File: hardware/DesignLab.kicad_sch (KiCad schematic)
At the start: 77 parts, among them J1 Micro_SD_Card_Det, J2 Conn_01x04_Female, J3 Conn_01x05, J5 Conn_01x05, P1 USB_C_Plug_USB2.0, Q1 DMG3415U-7, SW1 SW_DPDT_x2, SW11 SW_DPDT_x2, SW12 RESET, SW13 ON, SW14 VOL, SW15 BOOT, SW3 REC, U1 SPH0641LM4H, U10 MCP4018-xxxxLT, U2 RP2040, U3 QRE1113, U4 QRE1113, U5 QRE1113, U6 W25Q80DVSSIG, U7 PAM8302AASCR, U8 AP2112K-3.3, U9 QRE1113, Y1 12Mhz

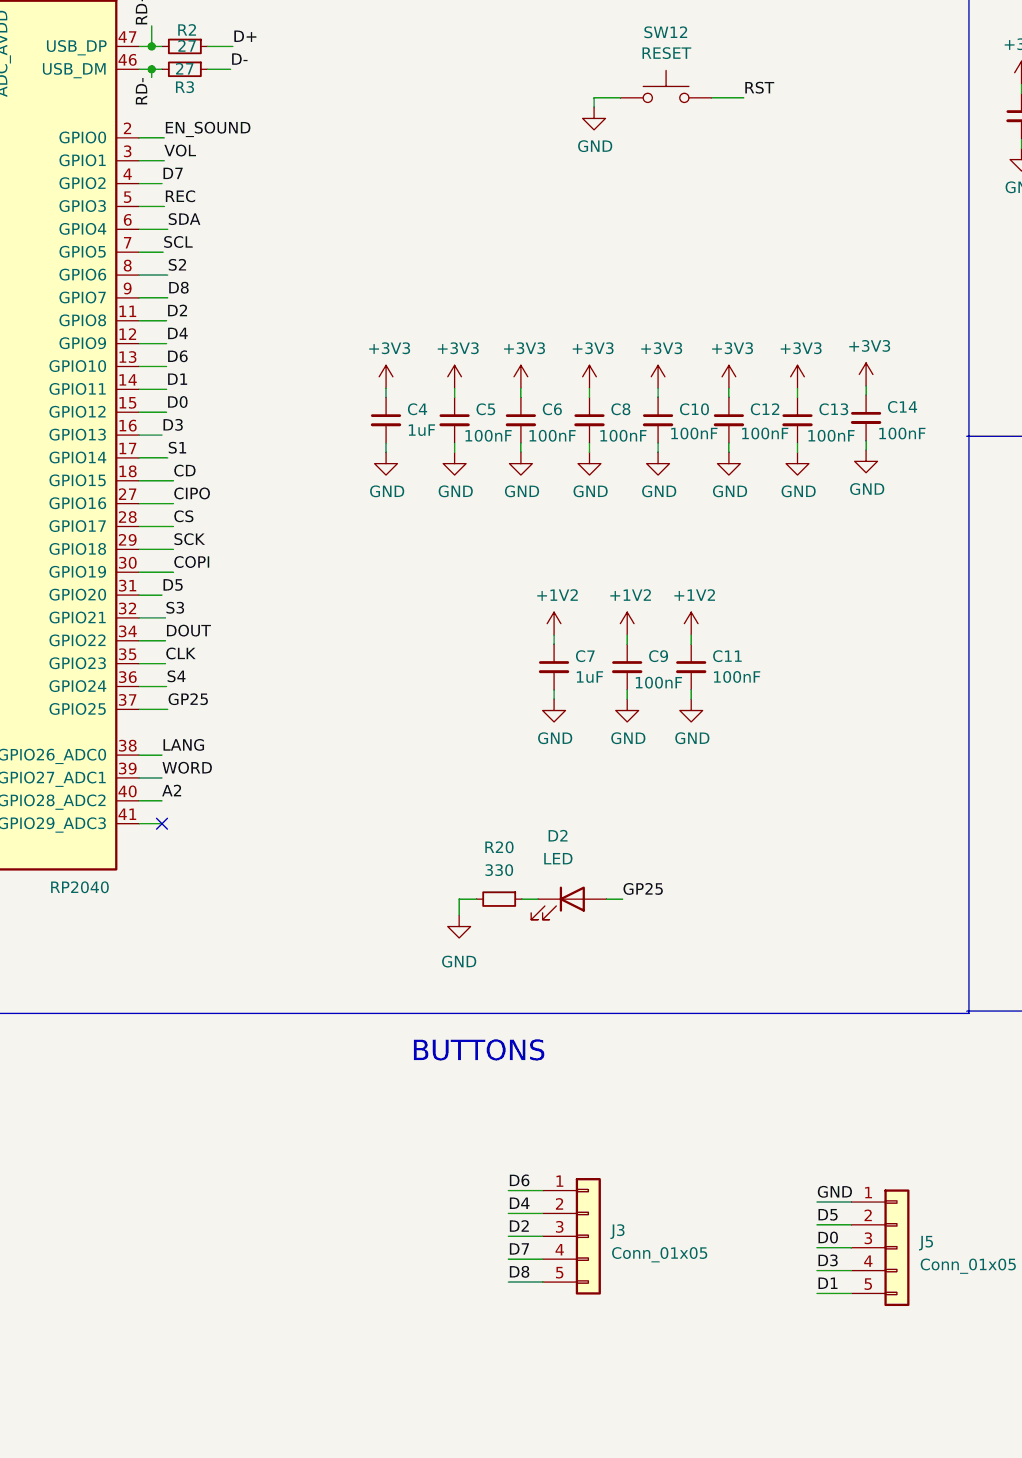
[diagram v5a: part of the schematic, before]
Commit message: PCB routing finished
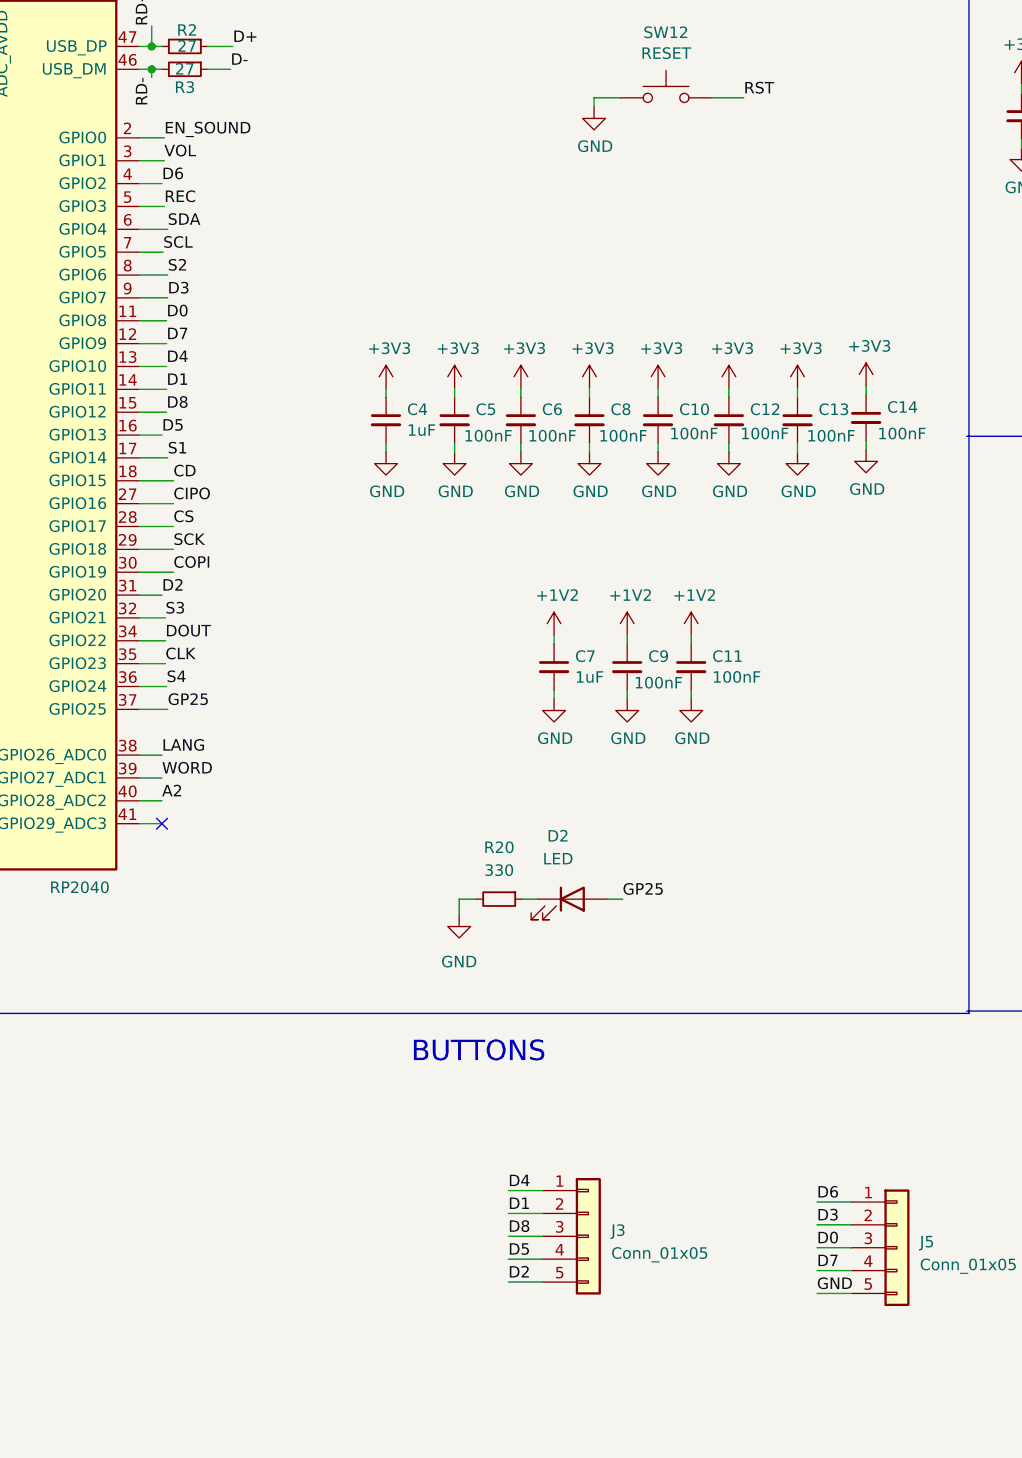
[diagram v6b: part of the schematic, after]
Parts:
- J3, J5: footprint (none) -> Connector_PinHeader_2.54mm:PinHeader_1x05_P2.54mm_Vertical
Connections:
- net D0: now also U2.11 (GPIO8); no longer U2.15 (GPIO12)
- net D1: now also J3.2 (Pin_2); no longer J5.5 (Pin_5)
- net D2: now also J3.5 (Pin_5), U2.31 (GPIO20); no longer J3.3 (Pin_3), U2.11 (GPIO8)
- net D3: now also J5.2 (Pin_2), U2.9 (GPIO7); no longer J5.4 (Pin_4), U2.16 (GPIO13)
- net D4: now also J3.1 (Pin_1), U2.13 (GPIO10); no longer J3.2 (Pin_2), U2.12 (GPIO9)
- net D5: now also J3.4 (Pin_4), U2.16 (GPIO13); no longer J5.2 (Pin_2), U2.31 (GPIO20)
- net D6: now also J5.1 (Pin_1), U2.4 (GPIO2); no longer J3.1 (Pin_1), U2.13 (GPIO10)
- net D7: now also J5.4 (Pin_4), U2.12 (GPIO9); no longer J3.4 (Pin_4), U2.4 (GPIO2)
- net D8: now also J3.3 (Pin_3), U2.15 (GPIO12); no longer J3.5 (Pin_5), U2.9 (GPIO7)
- net GND: now also J5.5 (Pin_5); no longer J5.1 (Pin_1)
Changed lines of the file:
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@@
     (effects (font (size 1.27 1.27)) (justify left bottom))
   )
-  (label "D0" (at 114.427 78.613 0) (fields_autoplaced)
+  (label "D8" (at 114.427 78.613 0) (fields_autoplaced)
     (effects (font (size 1.27 1.27)) (justify left bottom))
   )
@@
     (effects (font (size 1.27 1.27)) (justify left bottom))
   )
-  (label "D2" (at 114.427 68.453 0) (fields_autoplaced)
+  (label "D0" (at 114.427 68.453 0) (fields_autoplaced)
     (effects (font (size 1.27 1.27)) (justify left bottom))
   )
-  (label "D8" (at 152.4 175.26 0) (fields_autoplaced)
+  (label "D2" (at 152.4 175.26 0) (fields_autoplaced)
     (effects (font (size 1.27 1.27)) (justify left bottom))
   )
-  (label "D2" (at 152.4 170.18 0) (fields_autoplaced)
+  (label "D8" (at 152.4 170.18 0) (fields_autoplaced)
     (effects (font (size 1.27 1.27)) (justify left bottom))
   )
-  (label "D7" (at 152.4 172.72 0) (fields_autoplaced)
+  (label "D5" (at 152.4 172.72 0) (fields_autoplaced)
     (effects (font (size 1.27 1.27)) (justify left bottom))
   )
@@
     (effects (font (size 1.27 1.27)) (justify left bottom))
   )
-  (label "D3" (at 186.69 173.99 0) (fields_autoplaced)
+  (label "D7" (at 186.69 173.99 0) (fields_autoplaced)
     (effects (font (size 1.27 1.27)) (justify left bottom))
   )
@@
     (effects (font (size 1.27 1.27)) (justify left bottom))
   )
-  (label "D6" (at 152.4 165.1 0) (fields_autoplaced)
+  (label "D4" (at 152.4 165.1 0) (fields_autoplaced)
     (effects (font (size 1.27 1.27)) (justify left bottom))
   )
@@
     (effects (font (size 1.27 1.27)) (justify right bottom))
   )
-  (label "GND" (at 186.69 166.37 0) (fields_autoplaced)
+  (label "D6" (at 186.69 166.37 0) (fields_autoplaced)
     (effects (font (size 1.27 1.27)) (justify left bottom))
   )
@@
     (effects (font (size 1.27 1.27)) (justify left bottom))
   )
-  (label "D5" (at 186.69 168.91 0) (fields_autoplaced)
+  (label "D3" (at 186.69 168.91 0) (fields_autoplaced)
     (effects (font (size 1.27 1.27)) (justify left bottom))
   )
@@
     (effects (font (size 1.27 1.27)) (justify right bottom))
   )
-  (label "D7" (at 113.919 53.213 0) (fields_autoplaced)
+  (label "D6" (at 113.919 53.213 0) (fields_autoplaced)
     (effects (font (size 1.27 1.27)) (justify left bottom))
   )
-  (label "D4" (at 152.4 167.64 0) (fields_autoplaced)
+  (label "D1" (at 152.4 167.64 0) (fields_autoplaced)
     (effects (font (size 1.27 1.27)) (justify left bottom))
   )
@@
     (effects (font (size 1.27 1.27)) (justify left bottom))
   )
-  (label "D1" (at 186.69 176.53 0) (fields_autoplaced)
+  (label "GND" (at 186.69 176.53 0) (fields_autoplaced)
     (effects (font (size 1.27 1.27)) (justify left bottom))
   )
@@
     (effects (font (size 1.27 1.27)) (justify left bottom))
   )
-  (label "D4" (at 114.427 70.993 0) (fields_autoplaced)
+  (label "D7" (at 114.427 70.993 0) (fields_autoplaced)
     (effects (font (size 1.27 1.27)) (justify left bottom))
   )
@@
     (effects (font (size 1.27 1.27)) (justify left bottom))
   )
-  (label "D8" (at 114.554 65.913 0) (fields_autoplaced)
+  (label "D3" (at 114.554 65.913 0) (fields_autoplaced)
     (effects (font (size 1.27 1.27)) (justify left bottom))
   )
@@
     (effects (font (size 1.27 1.27)) (justify left bottom))
   )
-  (label "D5" (at 113.919 98.933 0) (fields_autoplaced)
+  (label "D2" (at 113.919 98.933 0) (fields_autoplaced)
     (effects (font (size 1.27 1.27)) (justify left bottom))
   )
@@
     (effects (font (size 1.27 1.27)) (justify left bottom))
   )
-  (label "D3" (at 113.919 81.153 0) (fields_autoplaced)
+  (label "D5" (at 113.919 81.153 0) (fields_autoplaced)
     (effects (font (size 1.27 1.27)) (justify left bottom))
   )
@@
     (effects (font (size 1.27 1.27)) (justify left bottom))
   )
-  (label "D6" (at 114.427 73.533 0) (fields_autoplaced)
+  (label "D4" (at 114.427 73.533 0) (fields_autoplaced)
     (effects (font (size 1.27 1.27)) (justify left bottom))
   )
@@
       (effects (font (size 1.27 1.27)) (justify left))
     )
-    (property "Footprint" "" (at 161.29 170.18 0)
+    (property "Footprint" "Connector_PinHeader_2.54mm:PinHeader_1x05_P2.54mm_Vertical" (at 161.29 170.18 0)
       (effects (font (size 1.27 1.27)) hide)
     )
@@
       (effects (font (size 1.27 1.27)) (justify left))
     )
-    (property "Footprint" "" (at 195.58 171.45 0)
+    (property "Footprint" "Connector_PinHeader_2.54mm:PinHeader_1x05_P2.54mm_Vertical" (at 195.58 171.45 0)
       (effects (font (size 1.27 1.27)) hide)
     )

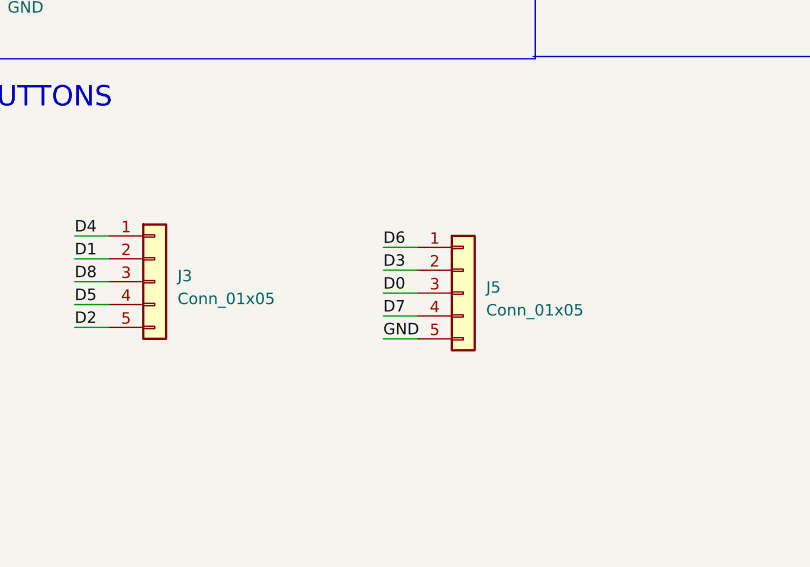
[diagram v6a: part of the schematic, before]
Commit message: Finished button PCBs
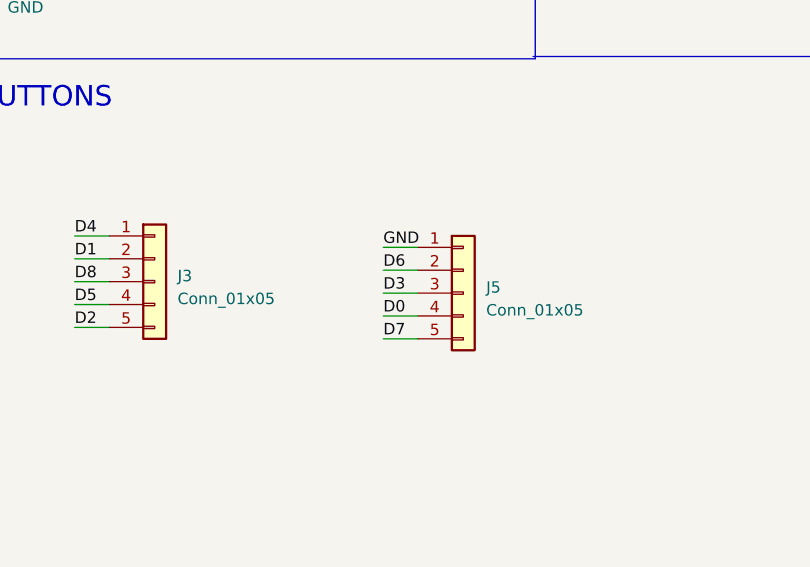
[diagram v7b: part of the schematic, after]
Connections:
- net D0: now also J5.4 (Pin_4); no longer J5.3 (Pin_3)
- net D3: now also J5.3 (Pin_3); no longer J5.2 (Pin_2)
- net D6: now also J5.2 (Pin_2); no longer J5.1 (Pin_1)
- net D7: now also J5.5 (Pin_5); no longer J5.4 (Pin_4)
- net GND: now also J5.1 (Pin_1); no longer J5.5 (Pin_5)
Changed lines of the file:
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@@
     (effects (font (size 1.27 1.27)) (justify left bottom))
   )
-  (label "D7" (at 186.69 173.99 0) (fields_autoplaced)
+  (label "D0" (at 186.69 173.99 0) (fields_autoplaced)
     (effects (font (size 1.27 1.27)) (justify left bottom))
   )
@@
     (effects (font (size 1.27 1.27)) (justify right bottom))
   )
-  (label "D6" (at 186.69 166.37 0) (fields_autoplaced)
+  (label "GND" (at 186.69 166.37 0) (fields_autoplaced)
     (effects (font (size 1.27 1.27)) (justify left bottom))
   )
@@
     (effects (font (size 1.27 1.27)) (justify left bottom))
   )
-  (label "D3" (at 186.69 168.91 0) (fields_autoplaced)
+  (label "D6" (at 186.69 168.91 0) (fields_autoplaced)
     (effects (font (size 1.27 1.27)) (justify left bottom))
   )
@@
     (effects (font (size 1.27 1.27)) (justify left bottom))
   )
-  (label "GND" (at 186.69 176.53 0) (fields_autoplaced)
+  (label "D7" (at 186.69 176.53 0) (fields_autoplaced)
     (effects (font (size 1.27 1.27)) (justify left bottom))
   )
@@
     (effects (font (size 1.27 1.27)) (justify left bottom))
   )
-  (label "D0" (at 186.69 171.45 0) (fields_autoplaced)
+  (label "D3" (at 186.69 171.45 0) (fields_autoplaced)
     (effects (font (size 1.27 1.27)) (justify left bottom))
   )

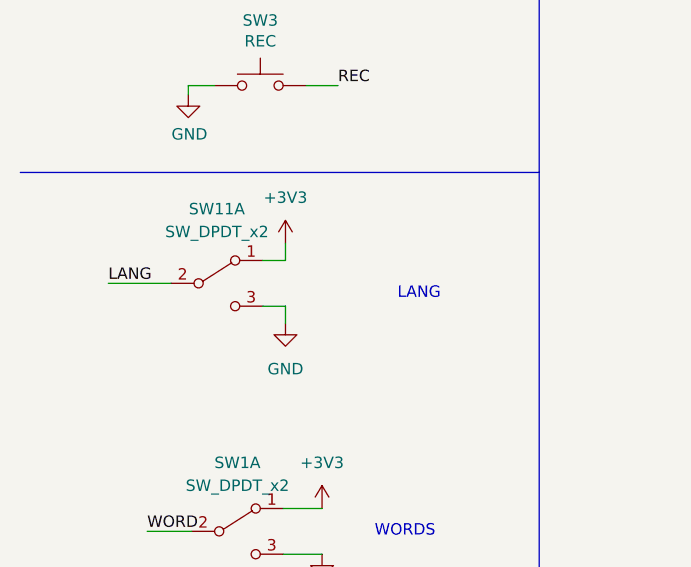
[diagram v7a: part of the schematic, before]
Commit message: Footprint of the switch lang changed
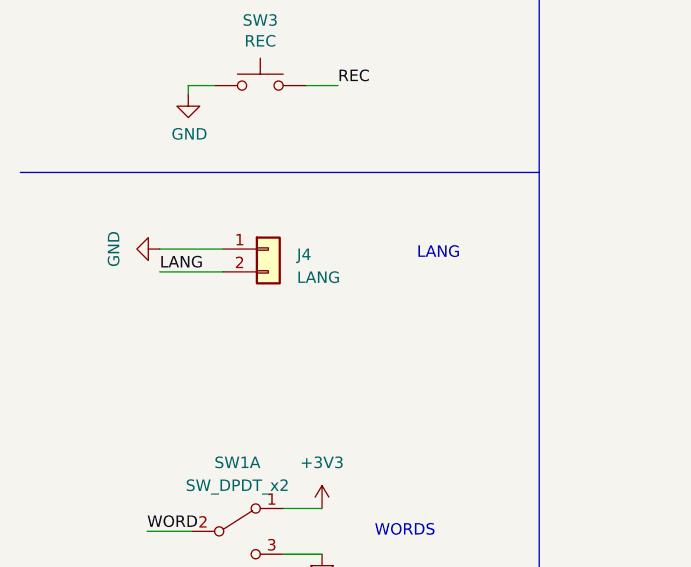
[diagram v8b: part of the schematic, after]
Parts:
- removed SW11: SW_DPDT_x2, Design:7829H-1-051LF, symbol Switch:SW_DPDT_x2
- added J4: LANG, Design:Swich, symbol Connector_Generic:Conn_01x02
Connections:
- net GND: now also J4.1 (Pin_1)
- net LANG: now also J4.2 (Pin_2)
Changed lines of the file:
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@@
     (stroke (width 0) (type default))
   )
-  (wire (pts (xy 22.225 239.395) (xy 29.21 239.395))
+  (wire (pts (xy 27.94 238.125) (xy 34.925 238.125))
     (stroke (width 0) (type default))
   )
@@
     (stroke (width 0) (type default))
   )
-  (wire (pts (xy 41.91 241.935) (xy 41.91 243.84))
-    (stroke (width 0) (type default))
-  )
   (wire (pts (xy 330.2 116.84) (xy 330.2 123.19))
     (stroke (width 0) (type default))
@@
     (stroke (width 0) (type default))
   )
-  (wire (pts (xy 39.37 236.855) (xy 41.91 236.855))
-    (stroke (width 0) (type default))
-  )
-  (wire (pts (xy 39.37 241.935) (xy 41.91 241.935))
-    (stroke (width 0) (type default))
-  )
   (wire (pts (xy 146.431 82.042) (xy 146.431 83.058))
     (stroke (width 0) (type default))
@@
     (stroke (width 0) (type default))
   )
-  (wire (pts (xy 41.91 236.855) (xy 41.91 234.95))
-    (stroke (width 0) (type default))
-  )
   (wire (pts (xy 175.006 43.688) (xy 178.562 43.688))
     (stroke (width 0) (type default))
@@
     (stroke (width 0) (type default))
   )
+  (wire (pts (xy 27.94 235.585) (xy 34.925 235.585))
+    (stroke (width 0) (type default))
+  )
   (wire (pts (xy 310.388 106.934) (xy 310.388 106.68))
     (stroke (width 0) (type default))
@@
     (effects (font (size 2.2606 2.2606)) (justify left bottom))
   )
-  (text "LANG" (at 54.356 241.3 0)
+  (text "LANG" (at 56.515 236.855 0)
     (effects (font (size 1.27 1.27)) (justify left bottom))
   )
@@
     (effects (font (size 1.27 1.27)) (justify left bottom))
   )
-  (label "LANG" (at 22.225 239.395 0) (fields_autoplaced)
+  (label "LANG" (at 27.94 238.125 0) (fields_autoplaced)
     (effects (font (size 1.27 1.27)) (justify left bottom))
   )
@@
     )
   )
-  (symbol (lib_id "power:+3V3") (at 41.91 234.95 0) (unit 1)
-    (in_bom yes) (on_board yes) (dnp no) (fields_autoplaced)
-    (property "Reference" "#PWR010" (at 41.91 238.76 0)
-      (effects (font (size 1.27 1.27)) hide)
-    )
-    (property "Value" "+3V3" (at 41.91 229.87 0)
-      (effects (font (size 1.27 1.27)))
-    )
-    (property "Footprint" "" (at 41.91 234.95 0)
-      (effects (font (size 1.27 1.27)) hide)
-    )
-    (property "Datasheet" "" (at 41.91 234.95 0)
-      (effects (font (size 1.27 1.27)) hide)
-    )
-    (pin "1")
-    (instances
-      (project "DesignLab"
-        (path "/3b4ee079-aeca-40f3-952f-1958b12a7eae"
-          (reference "#PWR010") (unit 1)
-        )
-      )
-    )
-  )
   (symbol (lib_id "power:VBUS") (at 400.05 26.543 0) (unit 1)
     (in_bom yes) (on_board yes) (dnp no)
@@
     )
   )
+  (symbol (lib_id "Connector_Generic:Conn_01x02") (at 40.005 235.585 0) (unit 1)
+    (in_bom yes) (on_board yes) (dnp no) (fields_autoplaced)
+    (property "Reference" "J4" (at 43.18 236.22 0)
+      (effects (font (size 1.27 1.27)) (justify left))
+    )
+    (property "Value" "LANG" (at 43.18 238.76 0)
+      (effects (font (size 1.27 1.27)) (justify left))
+    )
+    (property "Footprint" "Design:Swich" (at 40.005 235.585 0)
+      (effects (font (size 1.27 1.27)) hide)
+    )
+    (property "Datasheet" "~" (at 40.005 235.585 0)
+      (effects (font (size 1.27 1.27)) hide)
+    )
+    (pin "1")
+    (pin "2")
+    (instances
+      (project "DesignLab"
+        (path "/3b4ee079-aeca-40f3-952f-1958b12a7eae"
+          (reference "J4") (unit 1)
+        )
+      )
+    )
+  )
   (symbol (lib_id "power:+3V3") (at 161.417 75.946 0) (unit 1)
     (in_bom yes) (on_board yes) (dnp no)
@@
     )
   )
-  (symbol (lib_id "power:GND") (at 41.91 243.84 0) (unit 1)
+  (symbol (lib_id "power:GND") (at 27.94 235.585 270) (unit 1)
     (in_bom yes) (on_board yes) (dnp no) (fields_autoplaced)
-    (property "Reference" "#PWR011" (at 41.91 250.19 0)
+    (property "Reference" "#PWR011" (at 21.59 235.585 0)
       (effects (font (size 1.27 1.27)) hide)
     )
-    (property "Value" "GND" (at 41.91 248.92 0)
+    (property "Value" "GND" (at 22.86 235.585 0)
       (effects (font (size 1.27 1.27)))
     )
-    (property "Footprint" "" (at 41.91 243.84 0)
+    (property "Footprint" "" (at 27.94 235.585 0)
       (effects (font (size 1.27 1.27)) hide)
     )
-    (property "Datasheet" "" (at 41.91 243.84 0)
+    (property "Datasheet" "" (at 27.94 235.585 0)
       (effects (font (size 1.27 1.27)) hide)
     )
@@
         )
       )
-    )
-  )
-  (symbol (lib_id "Switch:SW_DPDT_x2") (at 34.29 239.395 0) (unit 1)
-    (in_bom yes) (on_board yes) (dnp no) (fields_autoplaced)
-    (property "Reference" "SW11" (at 34.29 231.14 0)
-      (effects (font (size 1.27 1.27)))
-    )
-    (property "Value" "SW_DPDT_x2" (at 34.29 233.68 0)
-      (effects (font (size 1.27 1.27)))
-    )
-    (property "Footprint" "Design:7829H-1-051LF" (at 34.29 239.395 0)
-      (effects (font (size 1.27 1.27)) hide)
-    )
-    (property "Datasheet" "https://www.mouser.mx/datasheet/2/54/7829-777130.pdf" (at 34.29 239.395 0)
-      (effects (font (size 1.27 1.27)) hide)
-    )
-    (property "Stock en EC" "No" (at 34.29 239.395 0)
-      (effects (font (size 1.27 1.27)) hide)
-    )
-    (property "manf#" "7829H-1-023LF" (at 34.29 239.395 0)
-      (effects (font (size 1.27 1.27)) hide)
-    )
-    (property "provedor" "MOUSER" (at 34.29 239.395 0)
-      (effects (font (size 1.27 1.27)) hide)
-    )
-    (pin "1")
-    (pin "2")
-    (pin "3")
-    (pin "4")
-    (pin "5")
-    (pin "6")
-    (instances
-      (project "DesignLab"
-        (path "/3b4ee079-aeca-40f3-952f-1958b12a7eae"
-          (reference "SW11") (unit 1)
-        )
-      )
